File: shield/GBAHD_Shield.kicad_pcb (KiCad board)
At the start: 2 copper layers, 79.5 x 64.4 mm, 70 parts, among them J1 Conn_01x40, J10 Conn_01x02, J11 Conn_01x05, J2 Conn_02x08_Top_Bottom, J3 Conn_01x20, J4 Conn_02x10_Top_Bottom, J5 Conn_01x34, J6 Conn_02x03_Odd_Even, J7 Conn_01x32, J8 Conn_01x05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

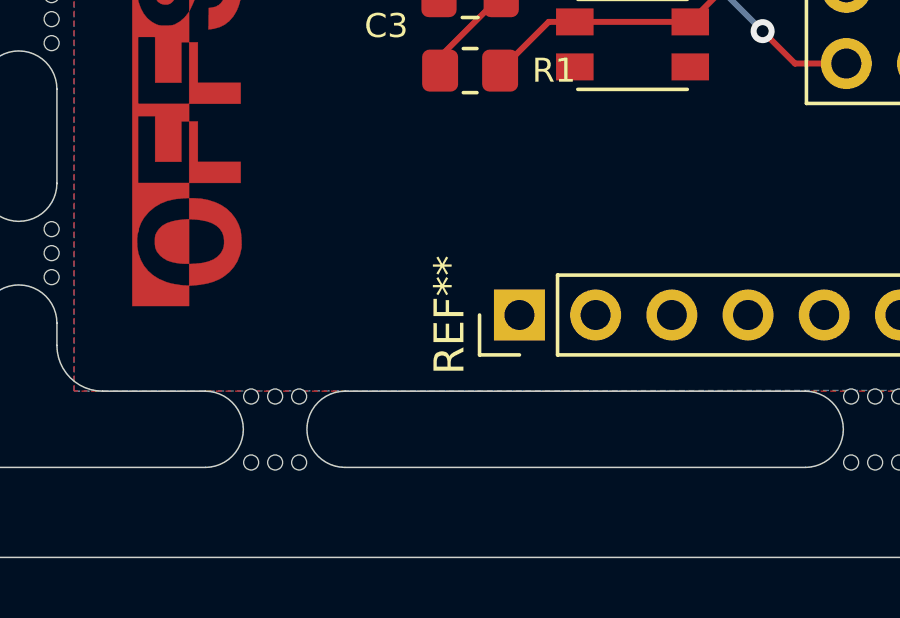
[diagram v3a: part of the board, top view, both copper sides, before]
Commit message: Added BOM, minor fixes
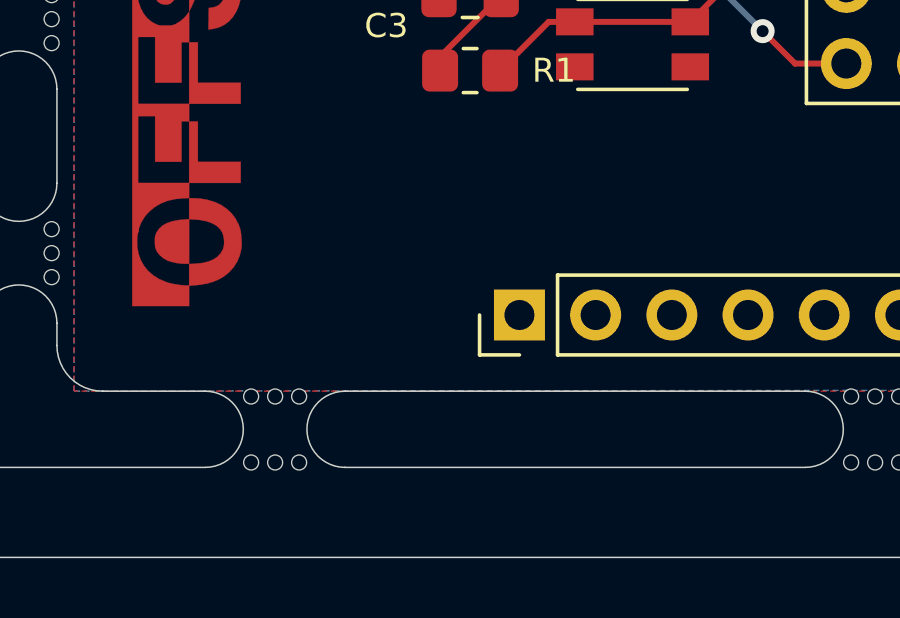
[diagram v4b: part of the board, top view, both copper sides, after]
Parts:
- removed mouse-bite-2.54mm-slot (x5): VAL**, Panelization:mouse-bite-2.54mm-slot
- added mousebite: VAL**, Panelization:mouse-bite-2.54mm-slot, F.Cu at (158.6, 45.7)
- added mousebite: VAL**, Panelization:mouse-bite-2.54mm-slot, F.Cu at (119.6, 45.7)
- added mousebite: VAL**, Panelization:mouse-bite-2.54mm-slot, F.Cu at (104.6, 45.7)
- added mousebite: VAL**, Panelization:mouse-bite-2.54mm-slot, F.Cu at (159.2, 101.6)
- added mousebite: VAL**, Panelization:mouse-bite-2.54mm-slot, F.Cu at (119.2, 101.6)
- renumbered REF** to EXP1, REF** to EXP2, HOLE_M3 to HOLEM3, mouse-bite-2.54mm-slot to mousebite

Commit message: Minor PCB changes
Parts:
- added REF**: OFFSET_LOGO_SILK_2.6mm, Raizu_OFFSET:OFFSET_LOGO_SILK_2.6mm, B.Cu at (99.5, 93.2)
- added REF**: OFFSET_LOGO_SILK_2.6mm, Raizu_OFFSET:OFFSET_LOGO_SILK_2.6mm, F.Cu at (100.1, 65.6)
- moved C3 8.84 mm to (132.3, 93.0), turned to 270 degrees
- moved R1 5.30 mm to (129.8, 93.0), turned to 270 degrees
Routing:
- net AT_RST: track 41.3 -> 48.6 mm
- net GBA_VCC: track 164.0 -> 168.1 mm
- net GND: track 151.5 -> 152.9 mm
